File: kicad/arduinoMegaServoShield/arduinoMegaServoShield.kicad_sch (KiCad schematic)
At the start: 9 parts, among them J1 Screw_Terminal_01x02, M1 Motor_Servo, M2 Motor_Servo, M3 Motor_Servo, M4 Motor_Servo, M5 Motor_Servo, M6 Motor_Servo

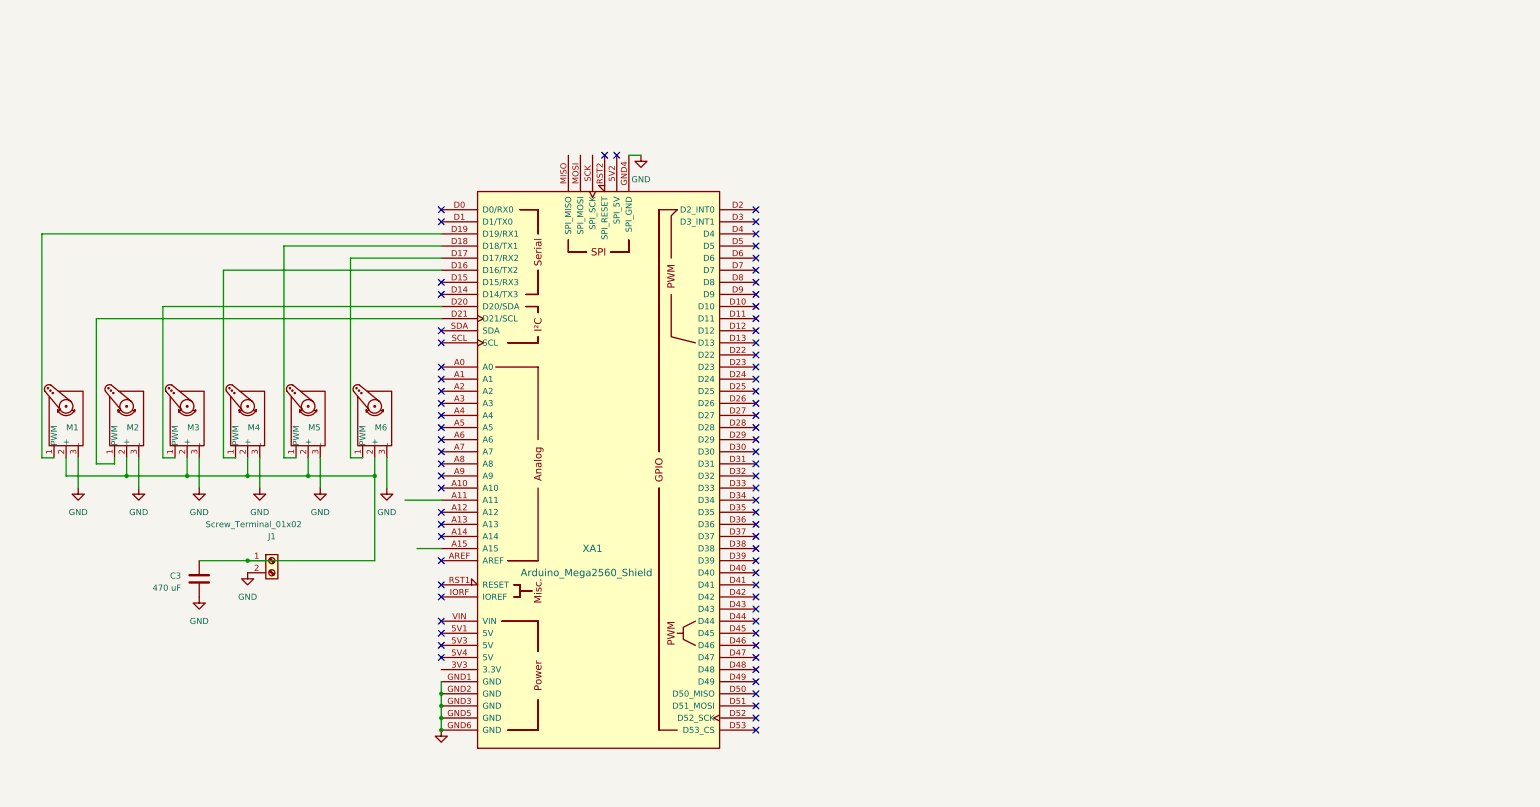
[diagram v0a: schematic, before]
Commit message: added all connectors
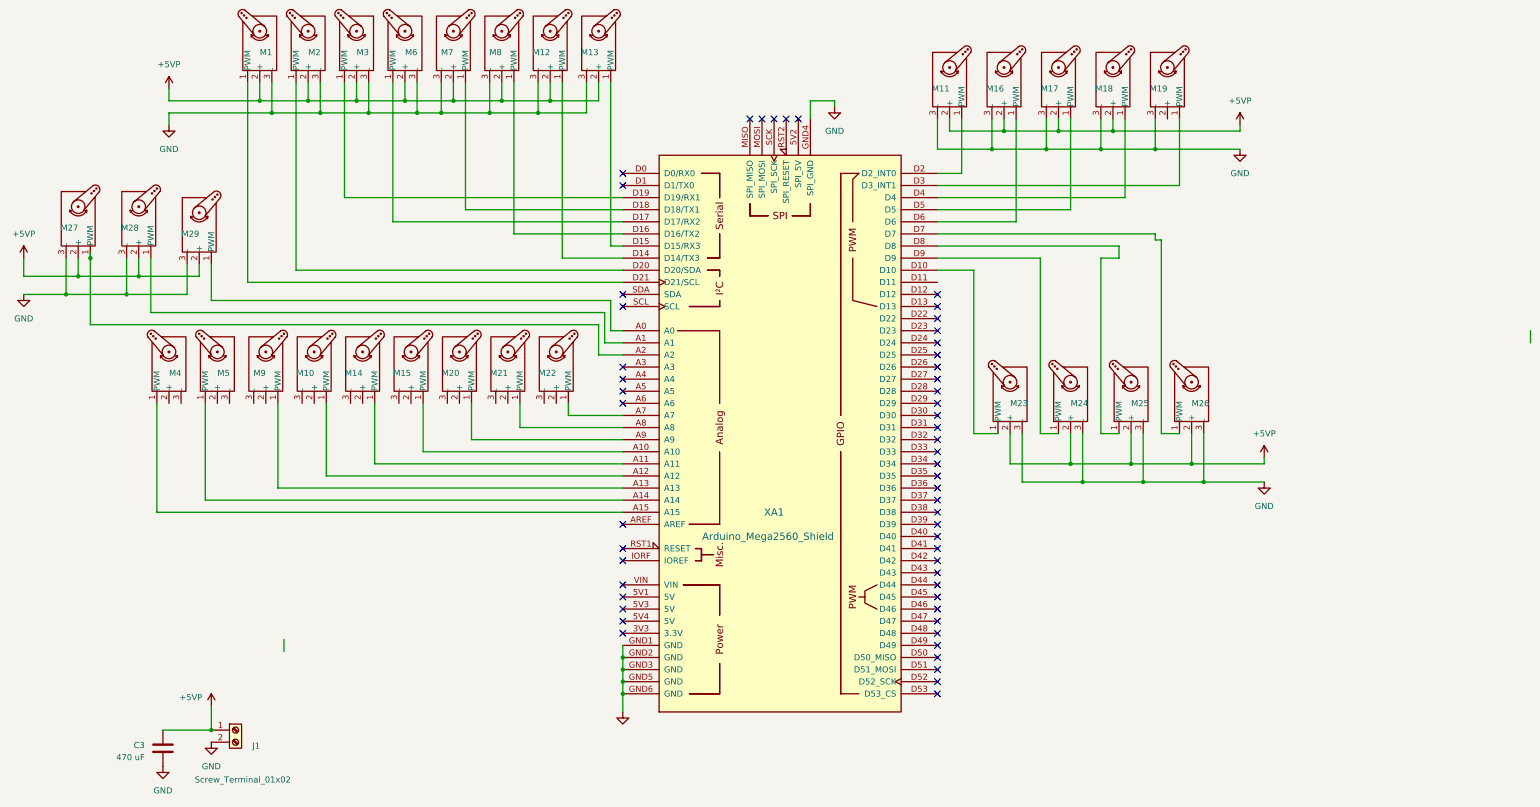
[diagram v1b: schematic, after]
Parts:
- added M10, M11, M12, M13, M14, M15, M16, M17, M18, M19, M20, M21, M22, M23, M24, M25, M26, M27, M28, M29, M7, M8, M9: Motor_Servo, Connector_PinHeader_2.54mm:PinHeader_1x03_P2.54mm_Vertical, symbol Motor:Motor_Servo
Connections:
- net GND: now also M11.3 (-), M12.3 (-), M13.3 (-), M16.3 (-), M17.3 (-), M18.3 (-), M19.3 (-), M23.3 (-), M24.3 (-), M25.3 (-), M26.3 (-), M27.3 (-), M28.3 (-), M29.3 (-), M7.3 (-), M8.3 (-); no longer M4.3 (-), M5.3 (-)
- net +5VP: now reaches C3.1, J1.1 (Pin_1), M1.2 (+), M2.2 (+), M3.2 (+), M6.2 (+)
- net +5VP: now also M11.2 (+), M12.2 (+), M13.2 (+), M16.2 (+), M17.2 (+), M18.2 (+), M23.2 (+), M24.2 (+), M25.2 (+), M26.2 (+), M27.2 (+), M28.2 (+), M29.2 (+), M7.2 (+), M8.2 (+); no longer M4.2 (+), M5.2 (+)
- net at M4.1 (PWM): now also XA1.A15; no longer XA1.D16 (D16/TX2)
- net at M5.1 (PWM): now also XA1.A14; no longer XA1.D18 (D18/TX1)
- net at M2.1 (PWM): now also XA1.D20 (D20/SDA); no longer XA1.D21 (D21/SCL)
- net at XA1.A0: now also M29.1 (PWM)
- net at XA1.A1: now also M28.1 (PWM)
- net at XA1.A10: now also M15.1 (PWM)
- net at XA1.A11: now also M14.1 (PWM)
- net at XA1.A12: now also M10.1 (PWM)
- net at XA1.A13: now also M9.1 (PWM)
- net at XA1.A2: now also M27.1 (PWM)
- net at XA1.A7: now also M22.1 (PWM)
- net at XA1.A8: now also M21.1 (PWM)
- net at XA1.A9: now also M20.1 (PWM)
- net at XA1.D10: now also M23.1 (PWM)
- net at XA1.D14 (D14/TX3): now also M12.1 (PWM)
- net at XA1.D15 (D15/RX3): now also M13.1 (PWM)
- net at XA1.D19 (D19/RX1): now also M3.1 (PWM); no longer M1.1 (PWM)
- net at XA1.D2 (D2_INT0): now also M11.1 (PWM)
- net at XA1.D3 (D3_INT1): now also M19.1 (PWM)
- net at XA1.D4: now also M18.1 (PWM)
- net at XA1.D5: now also M17.1 (PWM)
- net at XA1.D6: now also M16.1 (PWM)
- net at XA1.D7: now also M26.1 (PWM)
- net at XA1.D8: now also M25.1 (PWM)
- net at XA1.D9: now also M24.1 (PWM)
- new net: M7.1 (PWM), XA1.D18 (D18/TX1)
- new net: M8.1 (PWM), XA1.D16 (D16/TX2)
- new net: M1.1 (PWM), XA1.D21 (D21/SCL)
- no-connect marks 73 -> 55
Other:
- moved on the sheet: C3, J1, M1, M2, M3, M4, M5, M6, XA1

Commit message: improved layout
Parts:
- removed M15, M22, M24, M3: Motor_Servo, Connector_PinHeader_2.54mm:PinHeader_1x03_P2.54mm_Vertical, symbol Motor:Motor_Servo
- added M30, M31, M34, M35, M36, M37, M38, M39, M40, M41: Motor_Servo, Connector_PinHeader_2.54mm:PinHeader_1x03_P2.54mm_Vertical, symbol Motor:Motor_Servo
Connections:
- net +5VP: now also M4.2 (+); no longer M1.2 (+), M11.2 (+), M12.2 (+), M13.2 (+), M16.2 (+), M17.2 (+), M18.2 (+), M23.2 (+), M25.2 (+), M26.2 (+), M27.2 (+), M28.2 (+), M29.2 (+), M6.2 (+), M7.2 (+), M8.2 (+)
- net GND: now also M4.3 (-); no longer M1.3 (-), M11.3 (-), M12.3 (-), M13.3 (-), M16.3 (-), M17.3 (-), M18.3 (-), M19.3 (-), M23.3 (-), M25.3 (-), M26.3 (-), M27.3 (-), M28.3 (-), M29.3 (-), M6.3 (-), M7.3 (-), M8.3 (-), XA1.GND4 (SPI_GND)
- net at M6.1 (PWM): now also XA1.D24; no longer XA1.D17 (D17/RX2)
- net at M4.1 (PWM): now also XA1.D48; no longer XA1.A15
- net at M11.1 (PWM): now also XA1.D21 (D21/SCL); no longer XA1.D2 (D2_INT0)
- net at M10.1 (PWM): now also XA1.A7; no longer XA1.A12
- net at M16.1 (PWM): now also XA1.D36; no longer XA1.D6
- net at M9.1 (PWM): now also XA1.A6; no longer XA1.A13
- net at M14.1 (PWM): now also XA1.A10; no longer XA1.A11
- net at M28.1 (PWM): now also XA1.A3; no longer XA1.A1
- net at XA1.D10: now also M40.1 (PWM); no longer M23.1 (PWM)
- net at M29.1 (PWM): now also XA1.A4; no longer XA1.A0
- net at M17.1 (PWM): now also XA1.D4; no longer XA1.D5
- net at M13.1 (PWM): now also XA1.A9; no longer XA1.D15 (D15/RX3)
- net at M20.1 (PWM): now also XA1.A0; no longer XA1.A9
- net at M25.1 (PWM): now also XA1.D28; no longer XA1.D8
- net at M5.1 (PWM): now also XA1.A15; no longer XA1.A14
- net at M2.1 (PWM): now also XA1.D46; no longer XA1.D20 (D20/SDA)
- net at M18.1 (PWM): now also XA1.D5; no longer XA1.D4
- net at XA1.A8: now also M34.1 (PWM); no longer M21.1 (PWM)
- net at M7.1 (PWM): now also XA1.D32; no longer XA1.D18 (D18/TX1)
- net at M12.1 (PWM): now also XA1.D30; no longer XA1.D14 (D14/TX3)
- net at XA1.D7: now also M35.1 (PWM); no longer M26.1 (PWM)
- net at XA1.A5: now also M23.1 (PWM)
- net at XA1.D11: now also M39.1 (PWM)
- net at XA1.D12: now also M38.1 (PWM)
- net at XA1.D13: now also M37.1 (PWM)
- net at XA1.D16 (D16/TX2): no longer M8.1 (PWM)
- net at M1.1 (PWM): now also XA1.D22; no longer XA1.D21 (D21/SCL)
- net at XA1.D3 (D3_INT1): no longer M19.1 (PWM)
- net at XA1.D34: now also M30.1 (PWM)
- net at XA1.D38: now also M31.1 (PWM)
- net at XA1.D40: now also M8.1 (PWM)
- net at XA1.D9: now also M41.1 (PWM)
- new net: M36.1 (PWM), XA1.D8
- new net: M21.1 (PWM), XA1.A1
- new net: M26.1 (PWM), XA1.D20 (D20/SDA)
- new net: M19.1 (PWM), XA1.D6
- no-connect marks 55 -> 29
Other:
- moved on the sheet: M1, M10, M11, M12, M13, M14, M16, M17, M18, M19, M2, M20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

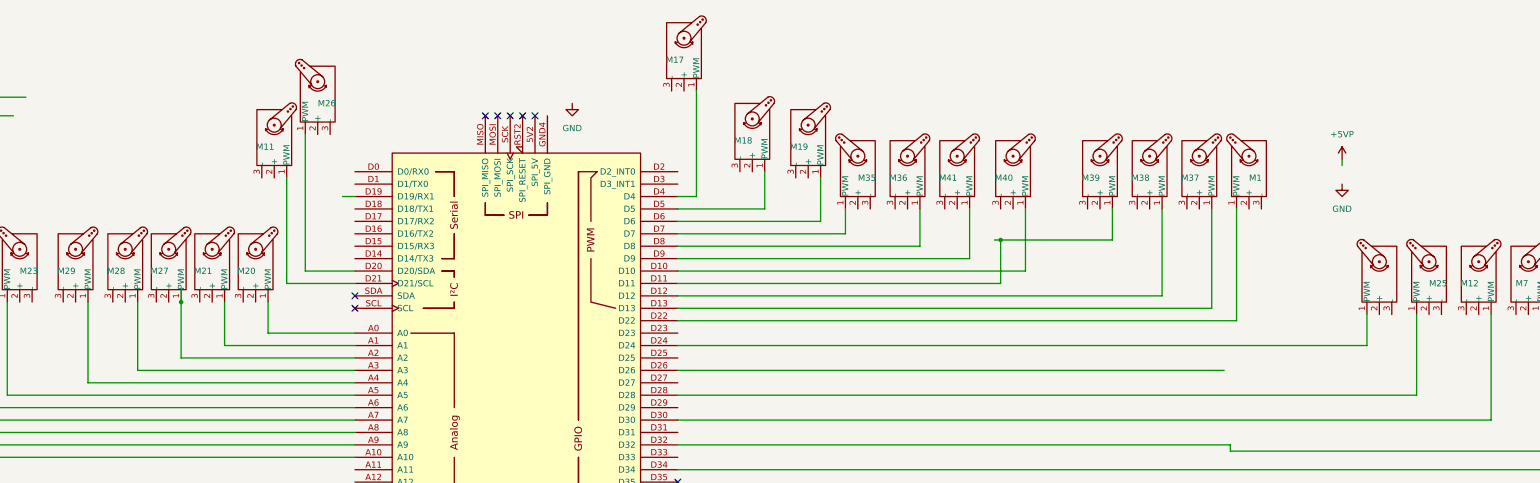
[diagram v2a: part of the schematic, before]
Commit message: added art criticism section
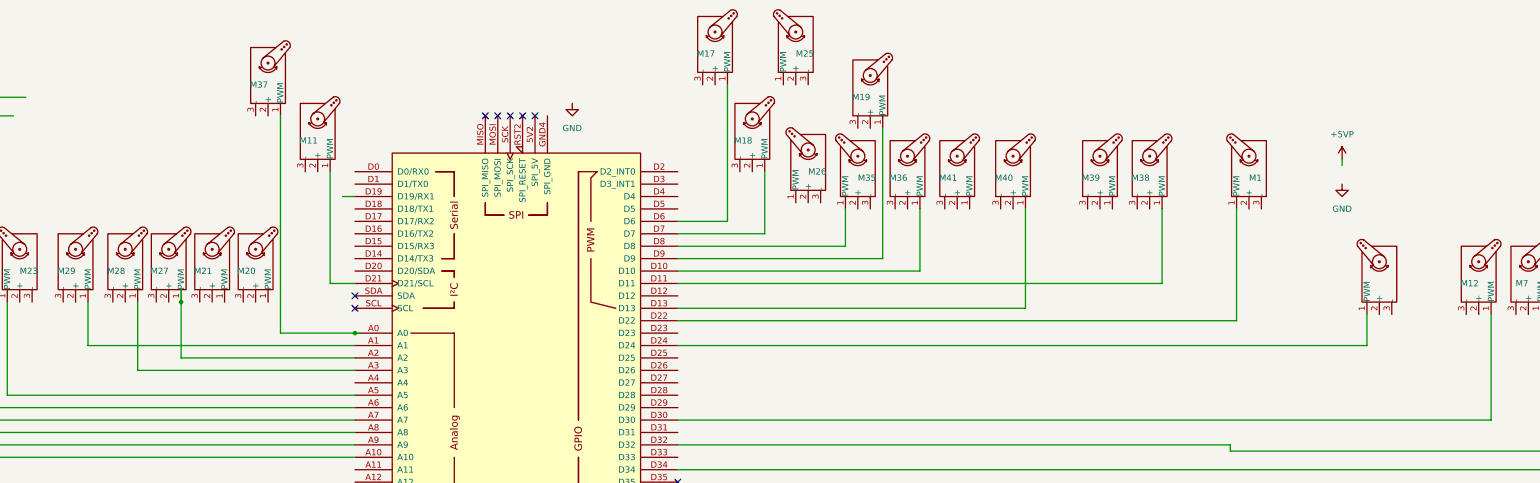
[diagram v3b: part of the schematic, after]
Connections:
- net at M35.1 (PWM): now also XA1.D8; no longer XA1.D7
- net at M40.1 (PWM): now also XA1.D13; no longer XA1.D10
- net at M29.1 (PWM): now also XA1.A1; no longer XA1.A4
- net at M17.1 (PWM): now also XA1.D6; no longer XA1.D4
- net at M38.1 (PWM): now also XA1.D11; no longer XA1.D12
- net at M20.1 (PWM): no longer XA1.A0
- net at M25.1 (PWM): no longer XA1.D28
- net at M37.1 (PWM): now also XA1.A0; no longer XA1.D13
- net at M18.1 (PWM): now also XA1.D7; no longer XA1.D5
- net at M36.1 (PWM): now also XA1.D10; no longer XA1.D8
- net at M41.1 (PWM): no longer XA1.D9
- net at M39.1 (PWM): no longer XA1.D11
- net at M21.1 (PWM): no longer XA1.A1
- net at M26.1 (PWM): no longer XA1.D20 (D20/SDA)
- net at M19.1 (PWM): now also XA1.D9; no longer XA1.D6
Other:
- moved on the sheet: M11, M17, M19, M25, M26, M37

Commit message: minor changes for Machine Lab 2026
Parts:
- removed M39, M41: Motor_Servo, Connector_PinHeader_2.54mm:PinHeader_1x03_P2.54mm_Vertical, symbol Motor:Motor_Servo
- added M15, M3: Motor_Servo, Connector_PinHeader_2.54mm:PinHeader_1x03_P2.54mm_Vertical, symbol Motor:Motor_Servo
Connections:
- net +5VP: now also M1.2 (+), M10.2 (+), M11.2 (+), M12.2 (+), M13.2 (+), M14.2 (+), M16.2 (+), M17.2 (+), M18.2 (+), M19.2 (+), M20.2 (+), M21.2 (+), M23.2 (+), M25.2 (+), M26.2 (+), M27.2 (+), M28.2 (+), M29.2 (+), M30.2 (+), M31.2 (+), M34.2 (+), M35.2 (+), M36.2 (+), M37.2 (+), M38.2 (+), M40.2 (+), M5.1 (PWM), M5.2 (+), M6.2 (+), M7.2 (+), M8.2 (+), M9.2 (+), XA1.A15, M15.2 (+), M3.2 (+)
- net GND: now also M1.3 (-), M10.3 (-), M11.3 (-), M12.3 (-), M13.3 (-), M14.3 (-), M16.3 (-), M17.3 (-), M18.3 (-), M19.3 (-), M20.3 (-), M21.3 (-), M23.3 (-), M25.3 (-), M26.3 (-), M27.3 (-), M28.3 (-), M29.3 (-), M30.3 (-), M31.3 (-), M34.3 (-), M35.3 (-), M36.3 (-), M37.3 (-), M38.3 (-), M40.3 (-), M5.3 (-), M6.3 (-), M7.3 (-), M8.3 (-), M9.3 (-), XA1.GND4 (SPI_GND), M15.3 (-), M3.3 (-)
- net at M6.1 (PWM): now also XA1.D16 (D16/TX2); no longer XA1.D24
- net at M11.1 (PWM): now also XA1.D14 (D14/TX3); no longer XA1.D21 (D21/SCL)
- net at M16.1 (PWM): now also XA1.A6; no longer XA1.D36
- net at M9.1 (PWM): now also XA1.A5; no longer XA1.A6
- net at M14.1 (PWM): now also XA1.A8; no longer XA1.A10
- net at M28.1 (PWM): now also XA1.D34; no longer XA1.A3
- net at M23.1 (PWM): now also XA1.D3 (D3_INT1); no longer XA1.A5
- net at M31.1 (PWM): now also XA1.D36; no longer XA1.D38
- net at M13.1 (PWM): now also XA1.A11; no longer XA1.A9
- net at M20.1 (PWM): now also XA1.A3
- net at M25.1 (PWM): now also XA1.D4
- net at M2.1 (PWM): now also XA1.D42; no longer XA1.D46
- net at M34.1 (PWM): now also XA1.A10; no longer XA1.A8
- net at M30.1 (PWM): now also XA1.A9; no longer XA1.D34
- net at M21.1 (PWM): now also XA1.A4
- net at XA1.D32: now also M3.1 (PWM); no longer M7.1 (PWM)
- net at M12.1 (PWM): now also XA1.D15 (D15/RX3); no longer XA1.D30
- net at M26.1 (PWM): now also XA1.D5
- net at XA1.D12: now also M15.1 (PWM)
- net at XA1.D17 (D17/RX2): now also M7.1 (PWM)
- net at M8.1 (PWM): now also XA1.D38; no longer XA1.D40
- no-connect marks 29 -> 49
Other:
- moved on the sheet: M1, M10, M11, M12, M13, M14, M16, M17, M18, M19, M2, M20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
